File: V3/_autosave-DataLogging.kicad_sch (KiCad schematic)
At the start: 5 parts, among them IC1 XTSD04GLGEAG, J7 THD2528-11SD-GF, SW4 SD_DUMP

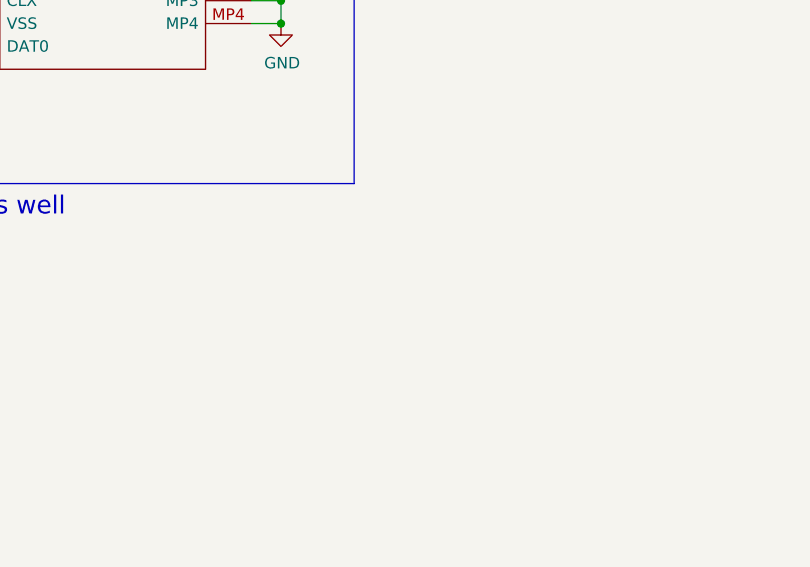
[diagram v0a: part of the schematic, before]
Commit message: New parts placed and routed
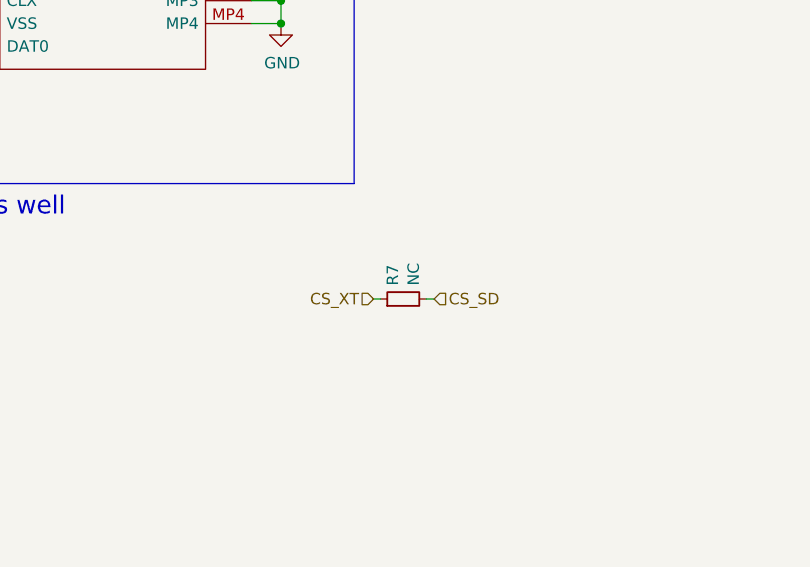
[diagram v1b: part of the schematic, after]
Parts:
- added R7: NC, Resistor_SMD:R_0603_1608Metric, symbol Device:R_Small
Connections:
- net CS_SD: now also R7.2
- net CS_XT: now also R7.1
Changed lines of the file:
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@@
+    (stroke (width 0) (type default) (color 0 0 0 0))
+  )
+  (wire (pts (xy 110.363 90.297) (xy 111.252 90.297))
     (stroke (width 0) (type default) (color 0 0 0 0))
   )
@@
   )
   (wire (pts (xy 202.438 107.696) (xy 202.438 111.76))
+    (stroke (width 0) (type default) (color 0 0 0 0))
+  )
+  (wire (pts (xy 104.521 90.297) (xy 105.283 90.297))
     (stroke (width 0) (type default) (color 0 0 0 0))
   )
@@
     (effects (font (size 1.27 1.27)) (justify right))
   )
+  (hierarchical_label "CS_XT" (shape input) (at 104.521 90.297 180)
+    (effects (font (size 1.27 1.27)) (justify right))
+  )
   (hierarchical_label "MISO_SD" (shape input) (at 57.912 62.23 180)
     (effects (font (size 1.27 1.27)) (justify right))
@@
   (hierarchical_label "CLK_SD" (shape input) (at 54.102 57.15 180)
     (effects (font (size 1.27 1.27)) (justify right))
+  )
+  (hierarchical_label "CS_SD" (shape input) (at 111.252 90.297 0)
+    (effects (font (size 1.27 1.27)) (justify left))
   )
   (hierarchical_label "MISO_SD" (shape input) (at 231.14 59.69 0)
@@
     (pin "1")
   )
+  (symbol (lib_id "Device:R_Small") (at 107.823 90.297 90) (unit 1)
+    (in_bom yes) (on_board yes)
+    (property "Reference" "R7" (id 0) (at 106.6546 88.7984 0)
+      (effects (font (size 1.27 1.27)) (justify left))
+    )
+    (property "Value" "NC" (id 1) (at 108.966 88.7984 0)
+      (effects (font (size 1.27 1.27)) (justify left))
+    )
+    (property "Footprint" "Resistor_SMD:R_0603_1608Metric" (id 2) (at 107.823 90.297 0)
+      (effects (font (size 1.27 1.27)) hide)
+    )
+    (property "Datasheet" "~" (id 3) (at 107.823 90.297 0)
+      (effects (font (size 1.27 1.27)) hide)
+    )
+    (pin "1")
+    (pin "2")
+  )
   (symbol (lib_id "XTSD04GLGEAG:XTSD04GLGEAG") (at 170.18 57.15 0) (unit 1)
